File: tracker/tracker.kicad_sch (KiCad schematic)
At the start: 5 parts, among them U1 XIAO-ESP32-C6-SMD, U2 LIS3DH

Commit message: yo
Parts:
- added C3: 100n, Package_QFP:TQFP-48_7x7mm_P0.5mm, symbol Device:C
- added Q2: Q_PMOS_GSD, Package_QFP:TQFP-44_10x10mm_P0.8mm, symbol Transistor_FET:Q_PMOS_GSD
- added R1, R3: 1M, symbol Device:R
- added R2: 100k, Package_QFP:TQFP-64_7x7mm_P0.4mm, symbol Device:R
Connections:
- net GND: now also C3.1, R3.1
- net at BT1.1 (+), U1.23 (VBAT): now also Q2.2 (S), R2.2
- net at U1.1 (D0): now also C3.2, R1.2, R3.2
- new net: Q2.1 (G), R2.1
- new net: Q2.3 (D), R1.1
- no-connect marks 23 -> 21

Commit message: added a nmos
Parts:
- added Q1: Q_NMOS_GSD, Package_QFP:TQFP-44_10x10mm_P0.8mm, symbol Transistor_FET:Q_NMOS_GSD
- added R4: 10k, symbol Device:R
- added R5: 100k, symbol Device:R
- R2: value 100k -> 1M
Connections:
- net GND: now also R3.2, Q1.3 (D), R5.2; no longer R3.1
- net at Q2.1 (G), R2.1: now also Q1.2 (S)
- net at BT1.1 (+), R2.2, U1.23 (VBAT): now also Q2.3 (D); no longer Q2.2 (S)
- net at C3.2, R1.2, U1.1 (D0): now also R3.1; no longer R3.2
- net at R1.1: now also Q2.2 (S); no longer Q2.3 (D)
- net at U1.2 (D1): now also R4.1
- new net: Q1.1 (G), R4.2, R5.1
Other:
- moved on the sheet: Q2

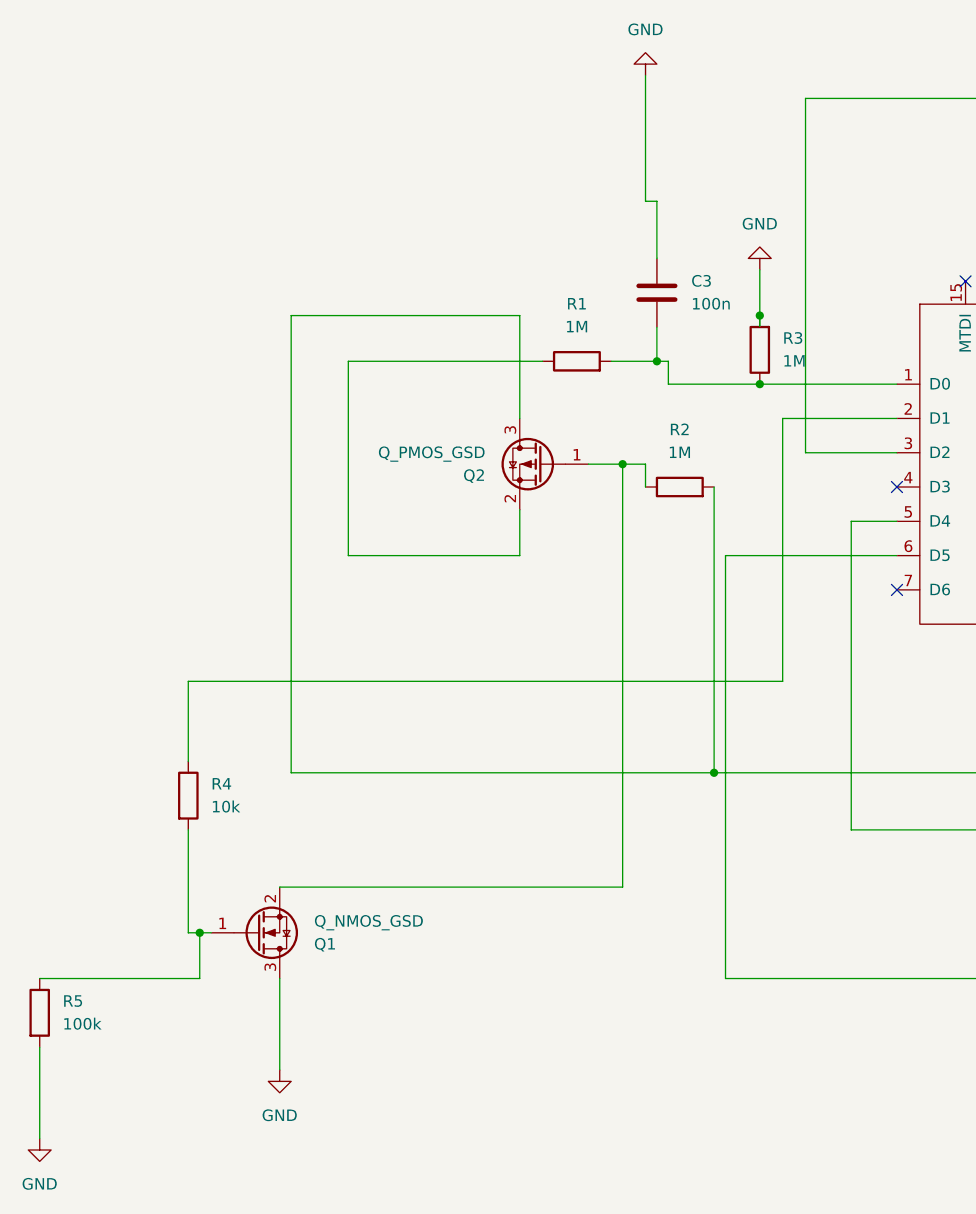
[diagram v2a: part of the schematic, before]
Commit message: added ina226
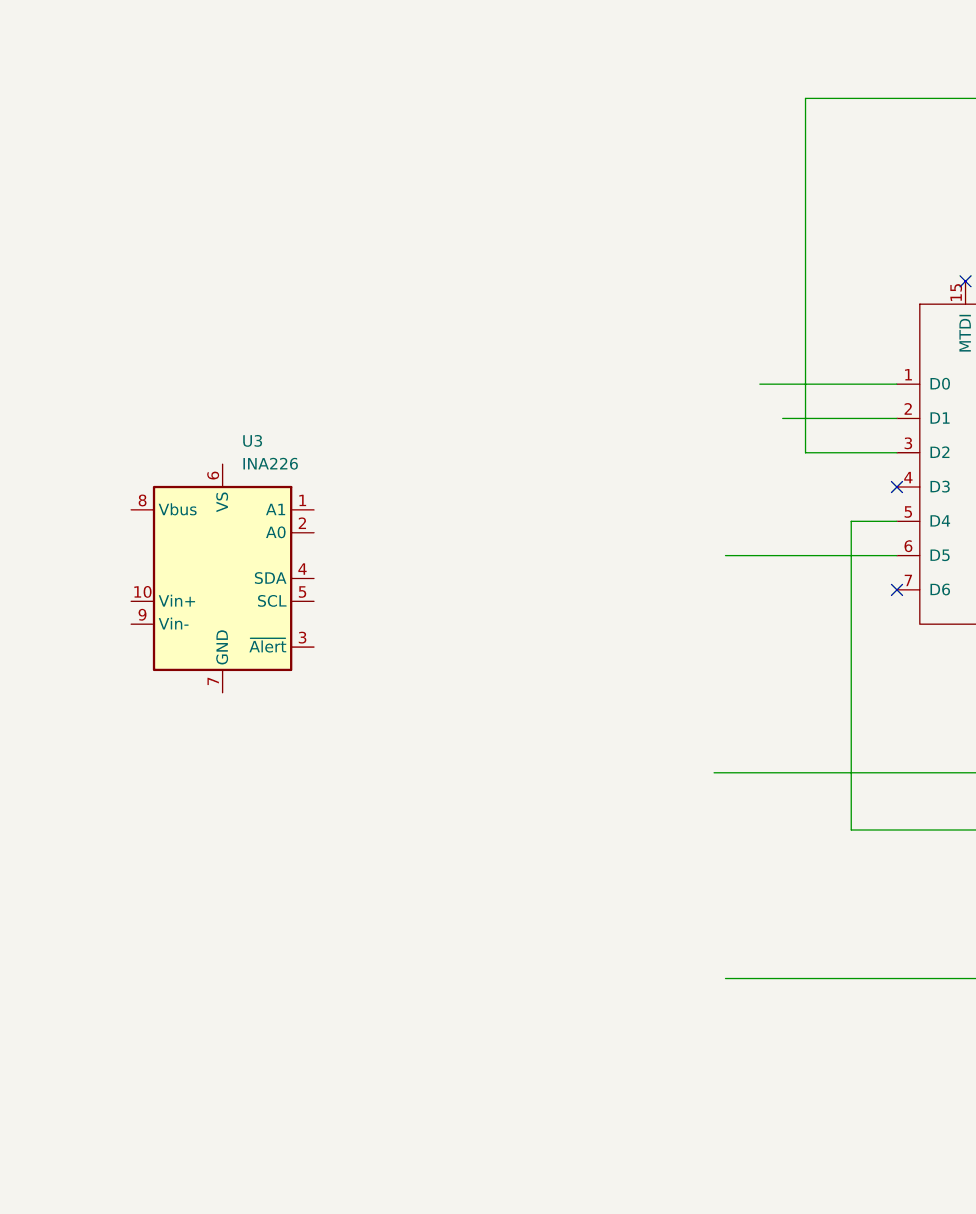
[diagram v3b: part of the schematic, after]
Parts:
- removed C3: 100n, Package_QFP:TQFP-48_7x7mm_P0.5mm, symbol Device:C
- removed Q1: Q_NMOS_GSD, Package_QFP:TQFP-44_10x10mm_P0.8mm, symbol Transistor_FET:Q_NMOS_GSD
- removed Q2: Q_PMOS_GSD, Package_QFP:TQFP-44_10x10mm_P0.8mm, symbol Transistor_FET:Q_PMOS_GSD
- removed R1, R3: 1M, symbol Device:R
- removed R2: 1M, Package_QFP:TQFP-64_7x7mm_P0.4mm, symbol Device:R
- removed R4: 10k, symbol Device:R
- removed R5: 100k, symbol Device:R
- added U3: INA226, Package_SO:TSSOP-10_3x3mm_P0.5mm, symbol Sensor_Energy:INA226
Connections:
- net at U1.6 (D5): no longer U2.4 (SPC)

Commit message: completed schematic
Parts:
- removed U3: INA226, Package_SO:TSSOP-10_3x3mm_P0.5mm, symbol Sensor_Energy:INA226
- added C3: 100p, C49851:MSOP-10_L3.0-W3.0-P0.50-LS5.0-BL, symbol Device:C
- added R1: 0.1, Resistor_SMD:R_2512_6332Metric, symbol Device:R
- added U3: TP4056_MICRO-USB_CHARGER_-_1A, TP4056_MICRO-USB_CHARGER_-_1A:MODULE_TP4056_MICRO-USB_CHARGER_-_1A, symbol TP4056_MICRO-USB_CHARGER_-_1A:TP4056_MICRO-USB_CHARGER_-_1A
- added U4: INA226AIDGSR, C49851:MSOP-10_L3.0-W3.0-P0.50-LS5.0-BL, symbol INA226:INA226AIDGSR
- C1: footprint Package_LGA:LGA-16_3x3mm_P0.5mm_LayoutBorder3x5y -> Capacitor_SMD:C_01005_0402Metric
- C2: footprint (none) -> Capacitor_SMD:C_01005_0402Metric
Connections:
- net GND: now also U1.13 (GND), U1.24 (GND), U2.10 (GND), U2.12 (GND), U2.5 (GND), C3.2, U3.OUT_N (OUT-), U4.1 (A1), U4.2 (A0), U4.7 (GND)
- net at C1.2, C2.2, U1.12 (3V3_OUT)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: now also C3.1, U4.6 (VS+)
- net at U1.23 (VBAT): now also R1.2, U4.8 (VBUS), U4.9 (VIN-); no longer BT1.1 (+)
- net at BT1.2 (-): now also U3.BAT_N (BAT-); no longer U1.24 (GND)
- net at U1.1 (D0): now also U4.3 (Alert)
- net at U1.5 (D4), U2.6 (SDI): now also U4.4 (SDA)
- net at U1.6 (D5): now also U2.4 (SPC), U4.5 (SCL)
- new net: R1.1, U3.OUT_P (OUT+), U4.10 (VIN+)
- new net: BT1.1 (+), U3.BAT_P (BAT+)
- no-connect marks 21 -> 22

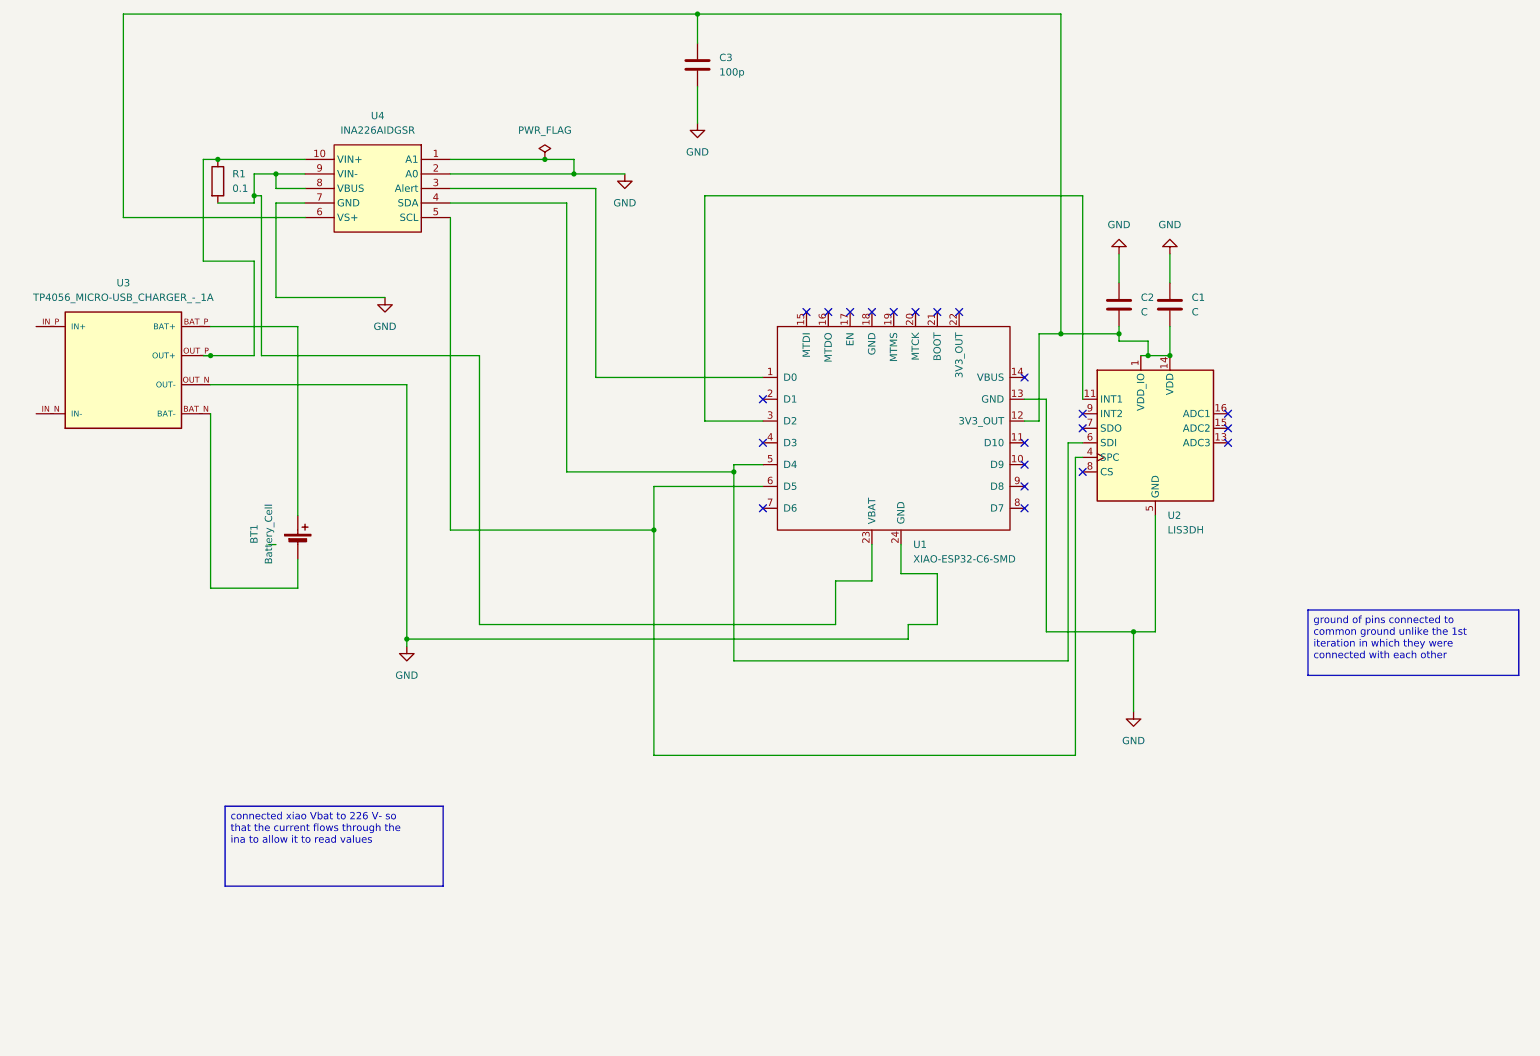
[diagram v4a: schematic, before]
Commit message: adding protection , charging ic
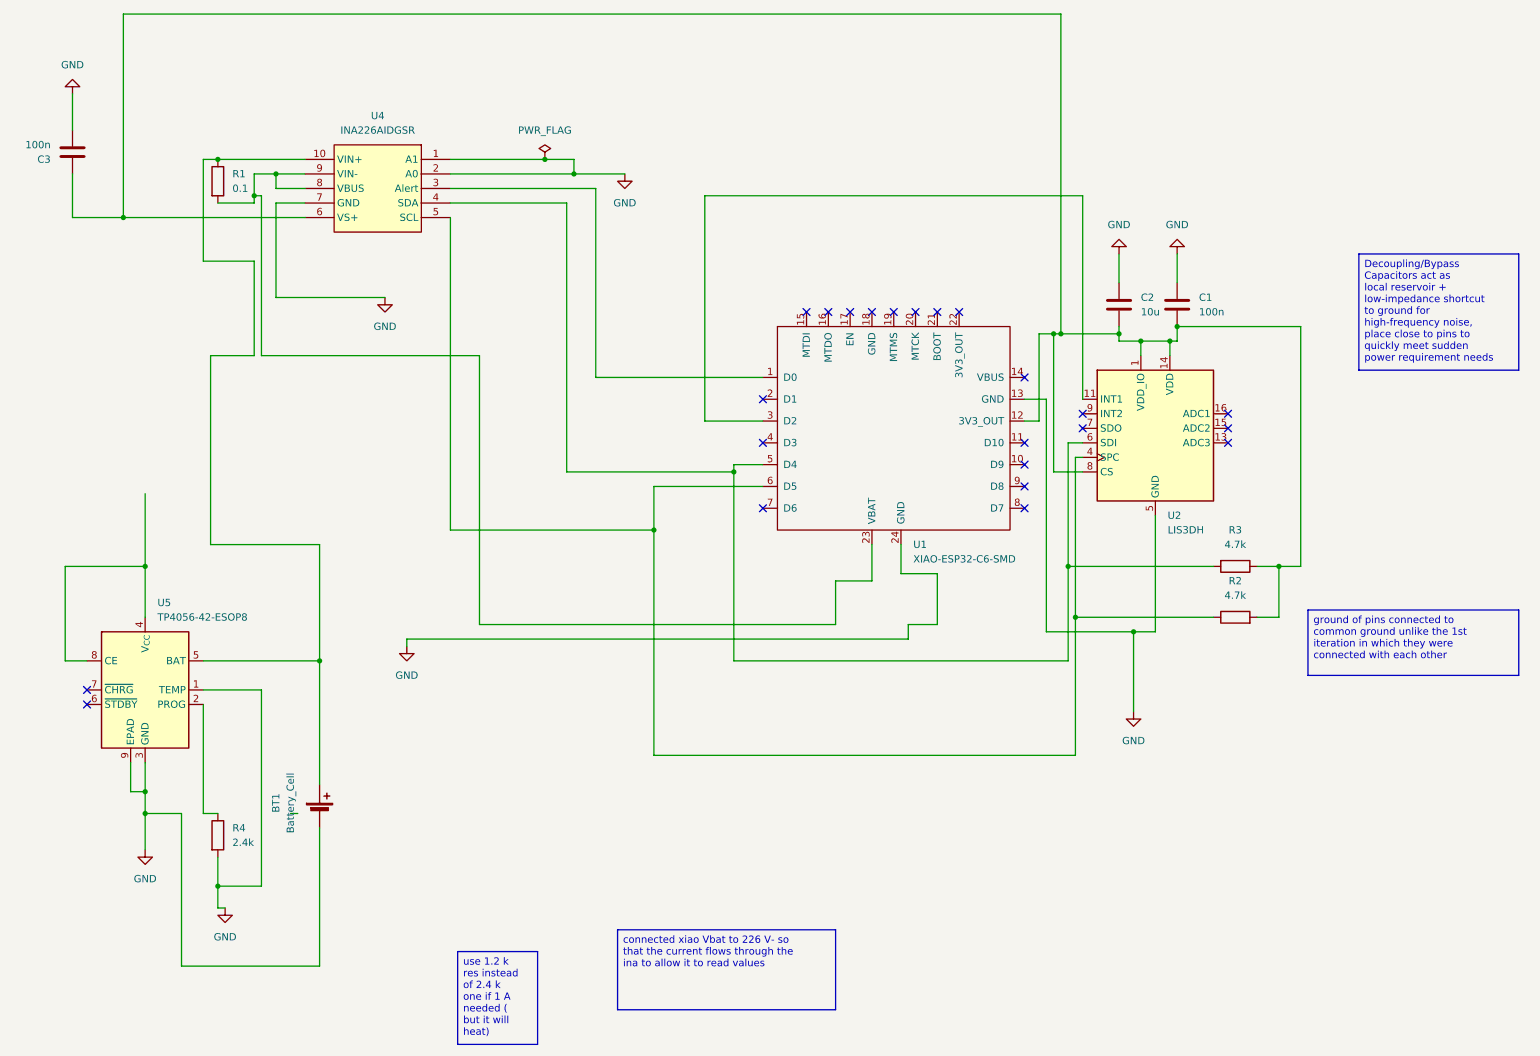
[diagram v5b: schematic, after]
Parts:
- removed U3: TP4056_MICRO-USB_CHARGER_-_1A, TP4056_MICRO-USB_CHARGER_-_1A:MODULE_TP4056_MICRO-USB_CHARGER_-_1A, symbol TP4056_MICRO-USB_CHARGER_-_1A:TP4056_MICRO-USB_CHARGER_-_1A
- added R2, R3: 4.7k, Resistor_SMD:R_0603_1608Metric, symbol Device:R
- added R4: 2.4k, Resistor_SMD:R_0603_1608Metric, symbol Device:R
- added U5: TP4056-42-ESOP8, Package_SO:SOIC-8-1EP_3.9x4.9mm_P1.27mm_EP2.41x3.3mm_ThermalVias, symbol Battery_Management:TP4056-42-ESOP8
- BT1: footprint Battery:BatteryClip_Keystone_54_D16-19mm -> Connector_JST:JST_PH_S2B-PH-K_1x02_P2.00mm_Horizontal
- C1: value C -> 100n; footprint Capacitor_SMD:C_01005_0402Metric -> Capacitor_SMD:C_0603_1608Metric
- C2: value C -> 10u; footprint Capacitor_SMD:C_01005_0402Metric -> Capacitor_SMD:C_0603_1608Metric
- C3: value 100p -> 100n; footprint C49851:MSOP-10_L3.0-W3.0-P0.50-LS5.0-BL -> Capacitor_SMD:C_0603_1608Metric
- U4: footprint C49851:MSOP-10_L3.0-W3.0-P0.50-LS5.0-BL -> Package_SO:TSSOP-10_3x3mm_P0.5mm
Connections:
- net GND: now also BT1.2 (-), R4.2, U5.1 (TEMP), U5.3 (GND), U5.9 (EPAD)
- net at C1.2, C2.2, C3.1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: now also U2.8 (CS), R2.2, R3.1
- net at R1.1, U4.10 (VIN+): now also BT1.1 (+), U5.5 (BAT)
- net at U1.5 (D4), U2.6 (SDI), U4.4 (SDA): now also R3.2
- net at U1.6 (D5), U2.4 (SPC), U4.5 (SCL): now also R2.1
- new net: R4.1, U5.2 (PROG)
- new net: U5.4 (V_{CC}), U5.8 (CE)
- no-connect marks 22 -> 23
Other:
- moved on the sheet: BT1, C1, C3

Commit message: friday update
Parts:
- removed BT1: Battery_Cell, Connector_JST:JST_PH_S2B-PH-K_1x02_P2.00mm_Horizontal, symbol Device:Battery_Cell
- removed R4: 2.4k, Resistor_SMD:R_0603_1608Metric, symbol Device:R
- removed U5: TP4056-42-ESOP8, Package_SO:SOIC-8-1EP_3.9x4.9mm_P1.27mm_EP2.41x3.3mm_ThermalVias, symbol Battery_Management:TP4056-42-ESOP8
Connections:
- net Charging_and_Battery/BAT+: now reaches R1.1, U4.10 (VIN+)
- no-connect marks 23 -> 21
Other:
- added sheet Charging_and_Battery (charging_and_battery.kicad_sch)

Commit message: added led's
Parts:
- U4: footprint Package_SO:TSSOP-10_3x3mm_P0.5mm -> Package_SO:MSOP-10_3x3mm_P0.5mm
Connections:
- net Shunt_Output: now reaches R1.2, U1.23 (VBAT), U4.8 (VBUS), U4.9 (VIN-)
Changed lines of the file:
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@@
+		)
+	)
+	(label "Shunt_Output"
+		(at 49.53 50.8 270)
+		(effects
+			(font
+				(size 1.27 1.27)
+			)
+			(justify right bottom)
 		)
 	)
@@
 			)
 		)
-		(property "Footprint" "Package_SO:TSSOP-10_3x3mm_P0.5mm"
+		(property "Footprint" "Package_SO:MSOP-10_3x3mm_P0.5mm"
 			(at 73.66 60.96 0)
 			(hide yes)
